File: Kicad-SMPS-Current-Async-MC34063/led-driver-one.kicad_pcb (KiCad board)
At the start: 2 copper layers, 35 x 40 mm, 40 parts, among them J1 Input 12V-30V, J2 Output, J3 Conn_01x01, U1 MC34063, U2 LM321

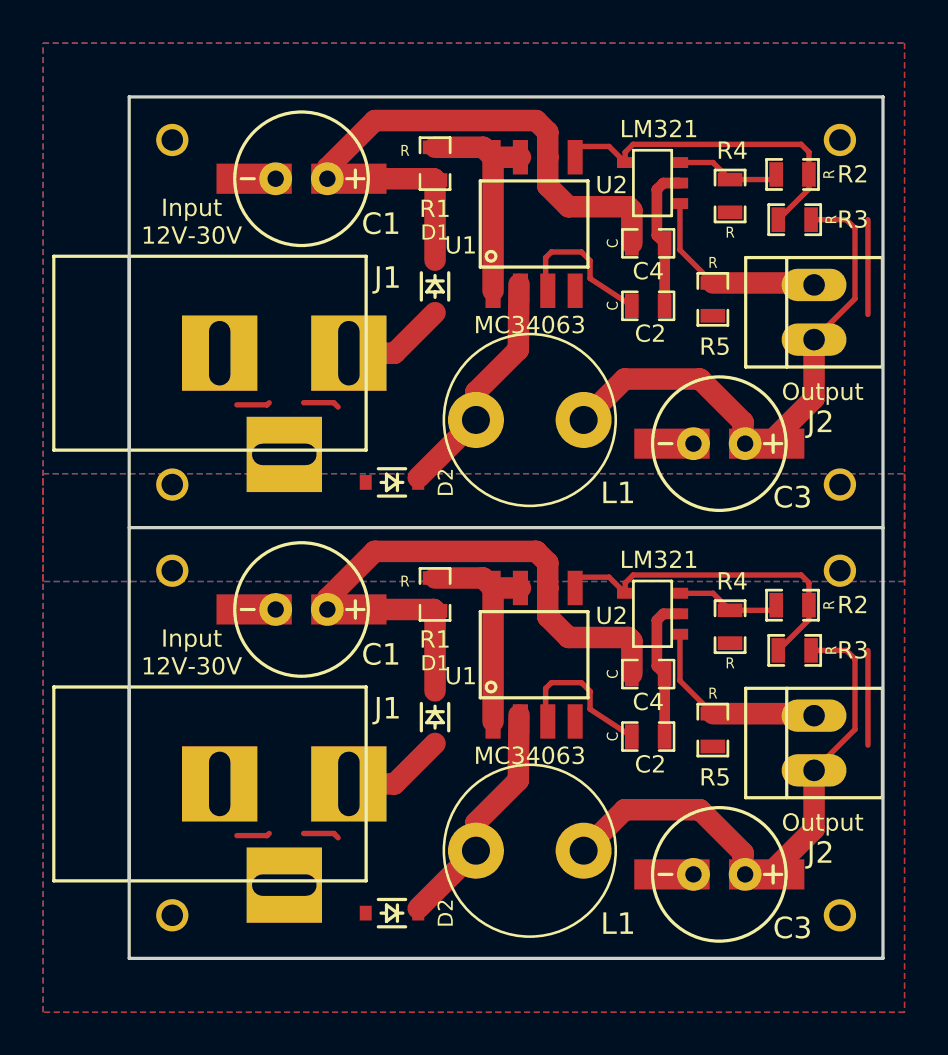
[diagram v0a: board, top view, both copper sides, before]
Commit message: Fix problem with current limiting resistor and also silk screen of diodes.
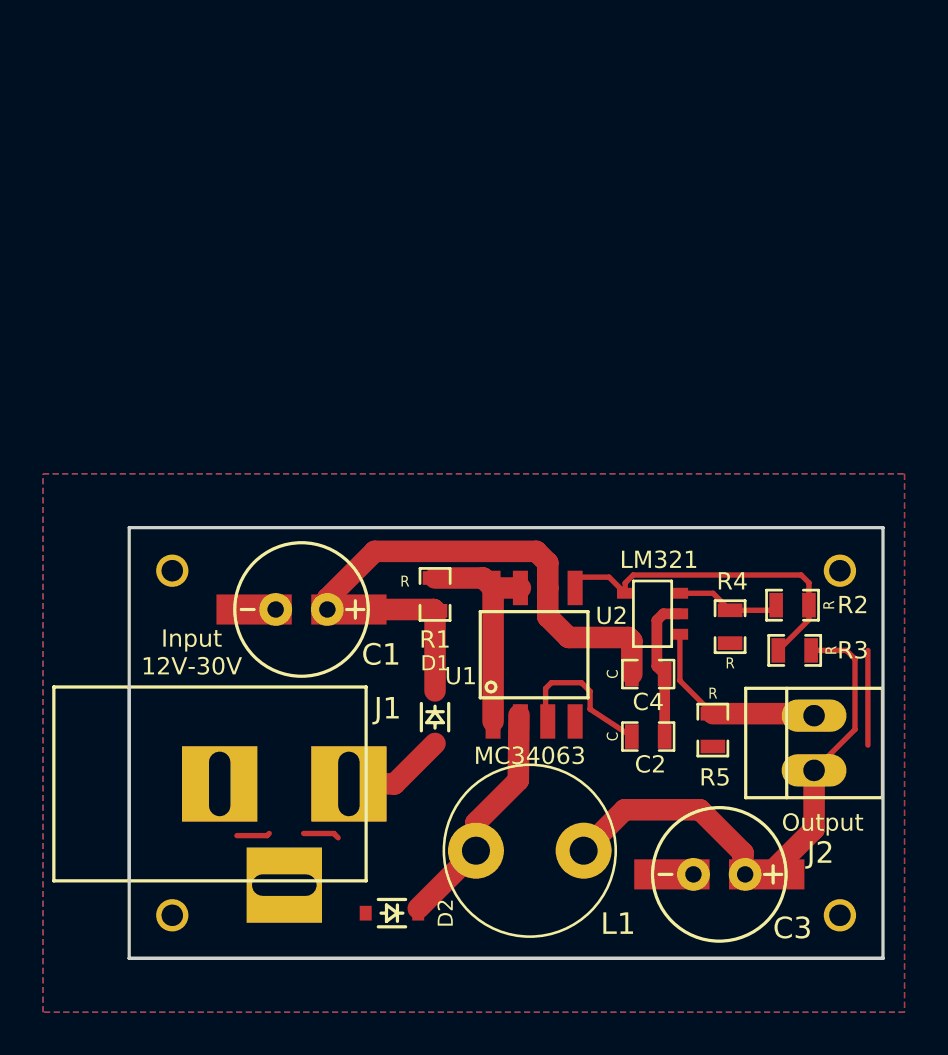
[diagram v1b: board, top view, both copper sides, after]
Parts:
- removed the C1 at (132.0, 91.3)
- removed the C2 at (148.1, 97.2)
- removed the C3 at (151.4, 103.6)
- removed the C4 at (148.1, 94.3)
- removed the D1 at (138.2, 96.3)
- removed the D2 at (136.2, 105.4)
- removed the J1 at (128.0, 99.4)
- removed the J2 at (155.8, 97.5)
- removed the J3 at (157.0, 105.5)
- removed the J3 at (126.0, 105.5)
- removed the J3 at (126.0, 89.5)
- removed the J3 at (157.0, 89.5)
- removed the L1 at (140.1, 102.5)
- removed the R1 at (138.2, 90.6)
- removed the R2 at (154.8, 91.1)
- removed the R3 at (154.9, 93.2)
- removed the R4 at (151.9, 92.1)
- removed the R5 at (151.1, 96.9)
- removed the U1 at (142.8, 93.4)
- removed the U2 at (148.3, 91.5)
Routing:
- net /Vcc: track 58.0 -> 29.0 mm
- net Net-(C3-Pad1): track 51.1 -> 25.5 mm
- net Net-(R2-Pad1): track 31.6 -> 15.8 mm
- net Net-(D2-Pad1): track 22.2 -> 11.1 mm
- net (no net): track 15.2 -> 4.40 mm
- net Net-(R1-Pad1): track 20.7 -> 10.4 mm
- net Net-(J2-Pad2): track 18.1 -> 9.06 mm
- net Net-(C2-Pad1): track 13.0 -> 6.52 mm
- net Net-(R2-Pad2): track 9.79 -> 4.89 mm
- net Net-(D1-Pad2): track 9.56 -> 4.78 mm
- net Earth: track 13.5 -> 9.97 mm
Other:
- board size 35 x 40 mm -> 35 x 20 mm
